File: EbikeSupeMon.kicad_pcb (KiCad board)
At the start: 2 copper layers, 47 parts, among them J1 USB_B_Micro, J2 Key switch, J3 Controller enable, J4 Bat IN, J5 Motor Out, Q1 DMP10H4D2S-7, SW1 IO_0, SW2 EN, SW3 USB-Reg_EN, U1 CP2102N-QFN28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

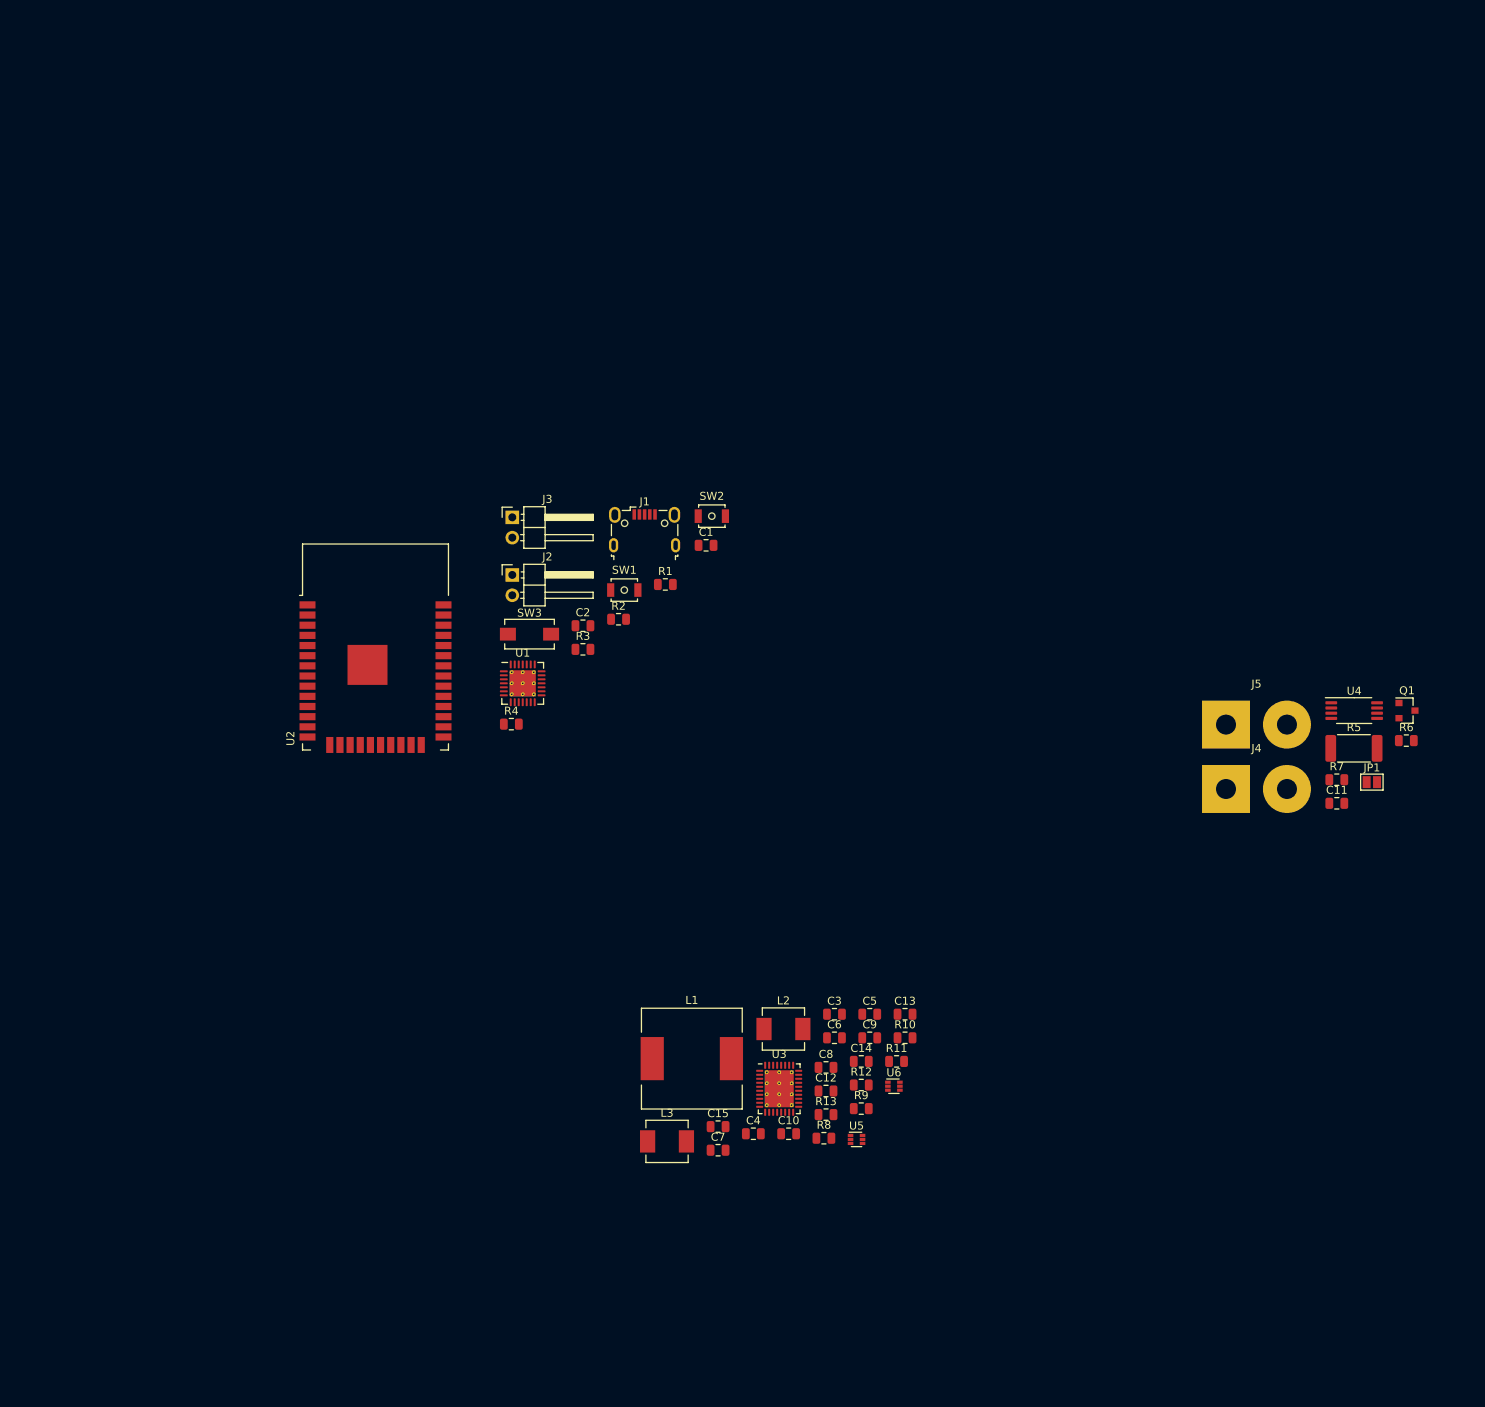
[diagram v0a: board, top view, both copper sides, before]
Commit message: 5v +3.3v reg layed out
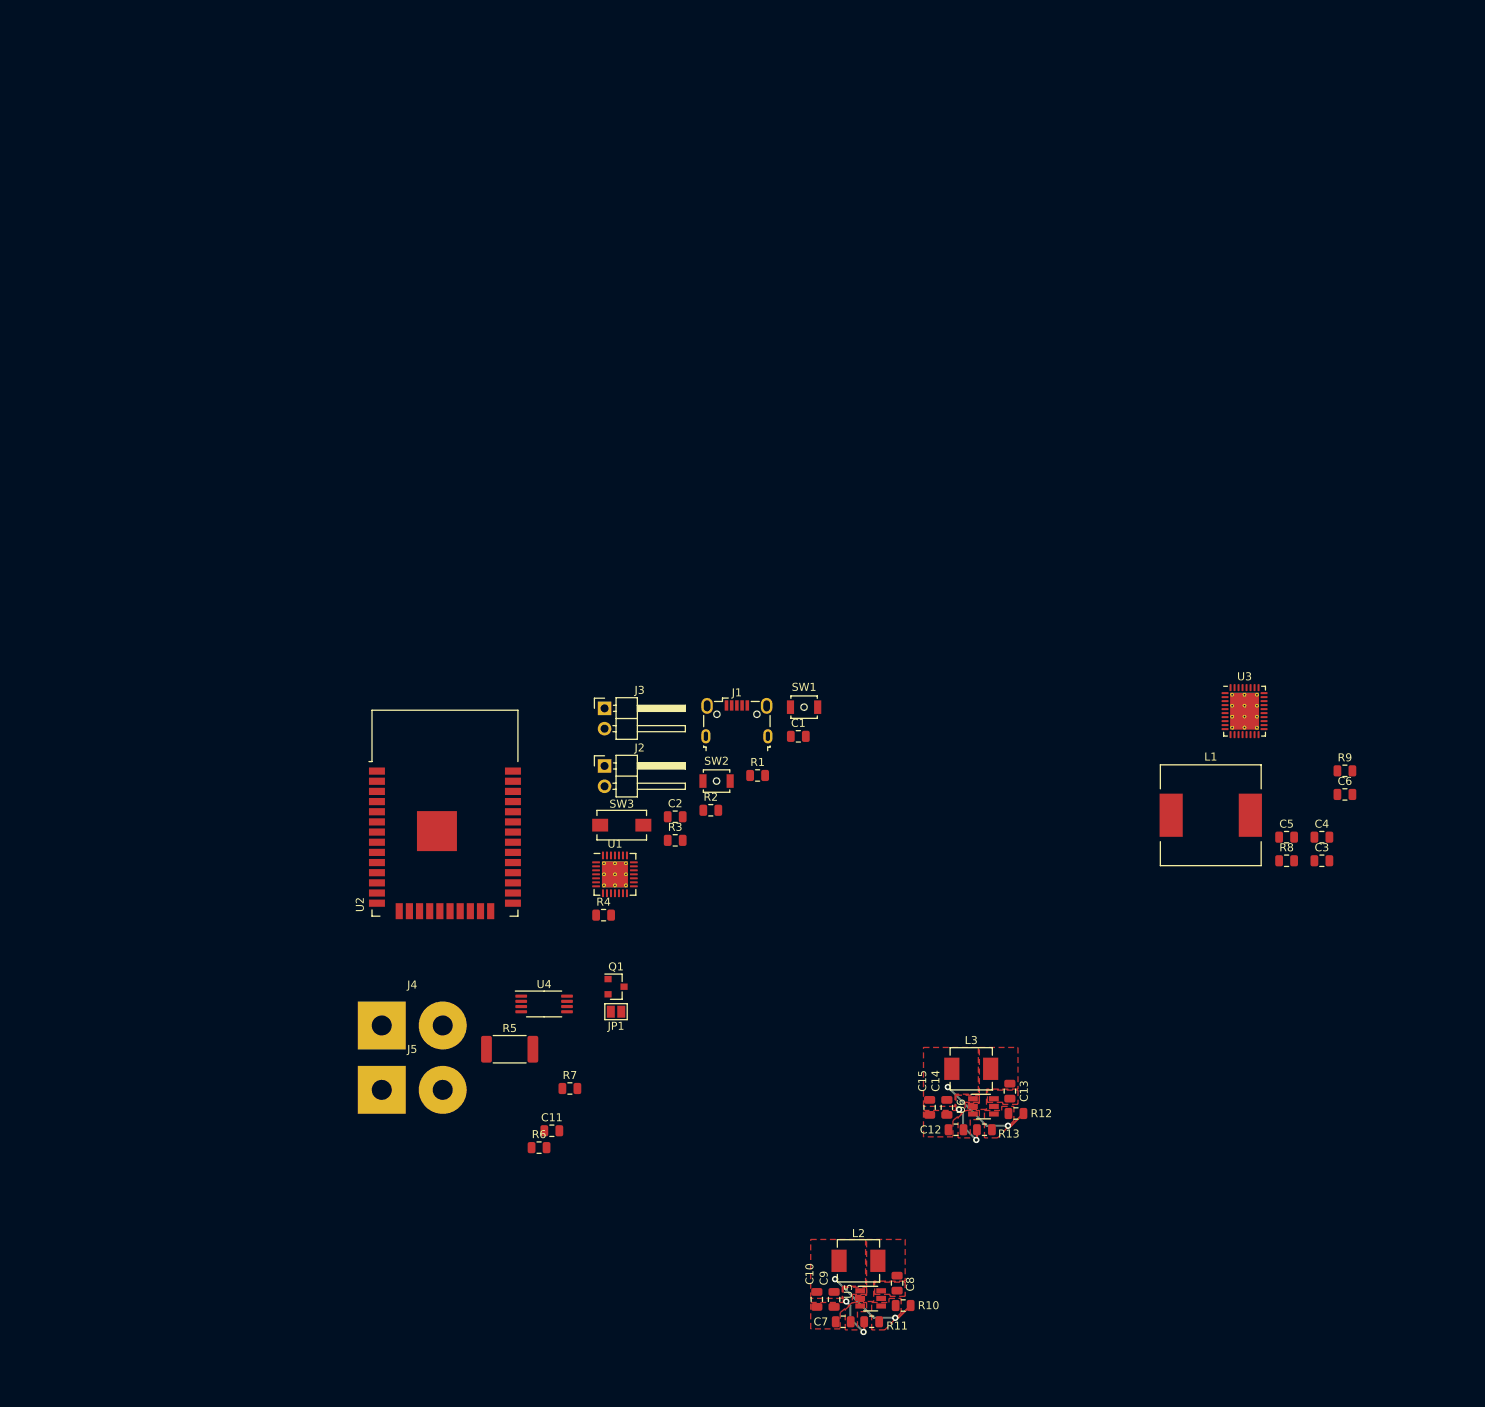
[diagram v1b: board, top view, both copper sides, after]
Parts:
- C10, C9: value 100nF X5R 6V -> 22uF X7R 10v
- C12: value 22uF X7R 10v -> 10uF 12V
- C13: value 22uF X7R 10v -> 100nF X5R 6V
- C8: value 10uF 12V -> 100nF X5R 6V
- R10: value 52.3k -> 31.6k
- R12: value 31.6k -> 52.3k
- U5, U6: footprint Package_TO_SOT_SMD:SOT-563 -> Package_TO_SOT_SMD:TSOT-23-6
- moved R6 119.8 mm to (112.3, 168.7)
- moved J5 115.0 mm to (92.7, 161.5)
- moved R5 112.0 mm to (108.7, 156.4)
- moved J4 109.6 mm to (92.7, 153.5)
- moved U4 107.7 mm to (113.0, 150.8)
- moved C11 106.3 mm to (113.9, 166.6)
- moved Q1 104.7 mm to (122.0, 148.6)
- moved R7 103.3 mm to (116.2, 161.3)
- moved JP1 98.7 mm to (122.0, 151.7), turned to 180 degrees
- moved C4 80.2 mm to (210.2, 129.9)
- moved U3 74.9 mm to (200.5, 114.2)
- moved R9 73.7 mm to (213.1, 121.6)
- moved L1 71.6 mm to (196.3, 127.2)
- moved C6 70.7 mm to (213.1, 124.6)
- moved R8 67.4 mm to (205.8, 132.9)
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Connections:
- C10 pad 1: Net-(C10-Pad1) -> +3V3
- C10 pad 2: Net-(C10-Pad2) -> GND
- C12 pad 1: +5V -> +12V
- C13 pad 1: +3V3 -> Net-(C13-Pad1)
- C13 pad 2: GND -> Net-(C13-Pad2)
- C15 pad 1: +3V3 -> +5V
- C8 pad 1: +12V -> Net-(C8-Pad1)
- C8 pad 2: GND -> Net-(C8-Pad2)
- C9 pad 1: Net-(C9-Pad1) -> +3V3
- C9 pad 2: Net-(C9-Pad2) -> GND
- J5 pad 2: (no net) -> Net-(J5-Pad2)
- L2 pad 1: Net-(C9-Pad2) -> Net-(C8-Pad2)
- L2 pad 2: +5V -> +3V3
- L3 pad 1: Net-(C10-Pad2) -> Net-(C13-Pad2)
- L3 pad 2: +3V3 -> +5V
- R10 pad 1: +5V -> +3V3
- R12 pad 1: +3V3 -> +5V
- U4 pad 3: (no net) -> Net-(R5-Pad3)
- U5 pad 1: +12V -> GND
- U5 pad 2: Net-(C9-Pad2) -> Net-(C8-Pad2)
- U5 pad 3: GND -> +12V
- U5 pad 4: Net-(C9-Pad1) -> Net-(R10-Pad2)
- U5 pad 6: Net-(R10-Pad2) -> Net-(C8-Pad1)
- U6 pad 1: +12V -> GND
- U6 pad 2: Net-(C10-Pad2) -> Net-(C13-Pad2)
- U6 pad 3: GND -> +12V
- U6 pad 4: Net-(C10-Pad1) -> Net-(R12-Pad2)
- U6 pad 6: Net-(R12-Pad2) -> Net-(C13-Pad1)
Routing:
- net +3V3: track 0.00 -> 12.1 mm, vias 0 -> 2
- net +5V: track 0.00 -> 12.1 mm, vias 0 -> 2
- net GND: track 0.00 -> 12.0 mm, vias 0 -> 4
- added copper zone on F.Cu, net +12V
- added copper zone on F.Cu, net +3V3
- added copper zone on F.Cu, net +5V
- added copper zone on F.Cu, net GND
- added copper zone on F.Cu, net Net-(C13-Pad1)
- added copper zone on F.Cu, net Net-(C13-Pad2)
- added copper zone on F.Cu, net Net-(C8-Pad1)
- added copper zone on F.Cu, net Net-(C8-Pad2)
- added copper zone on F.Cu, net Net-(R10-Pad2)
- added copper zone on F.Cu, net Net-(R12-Pad2)
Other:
- net class thin added: clearance 0.05, trace_width 0.2, via_dia 0.65, via_drill 0.3
- rule pad_to_mask_clearance: 0.05 -> 0.025
- rule trace_min: 0.2 -> 0.1

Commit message: 12vReg done
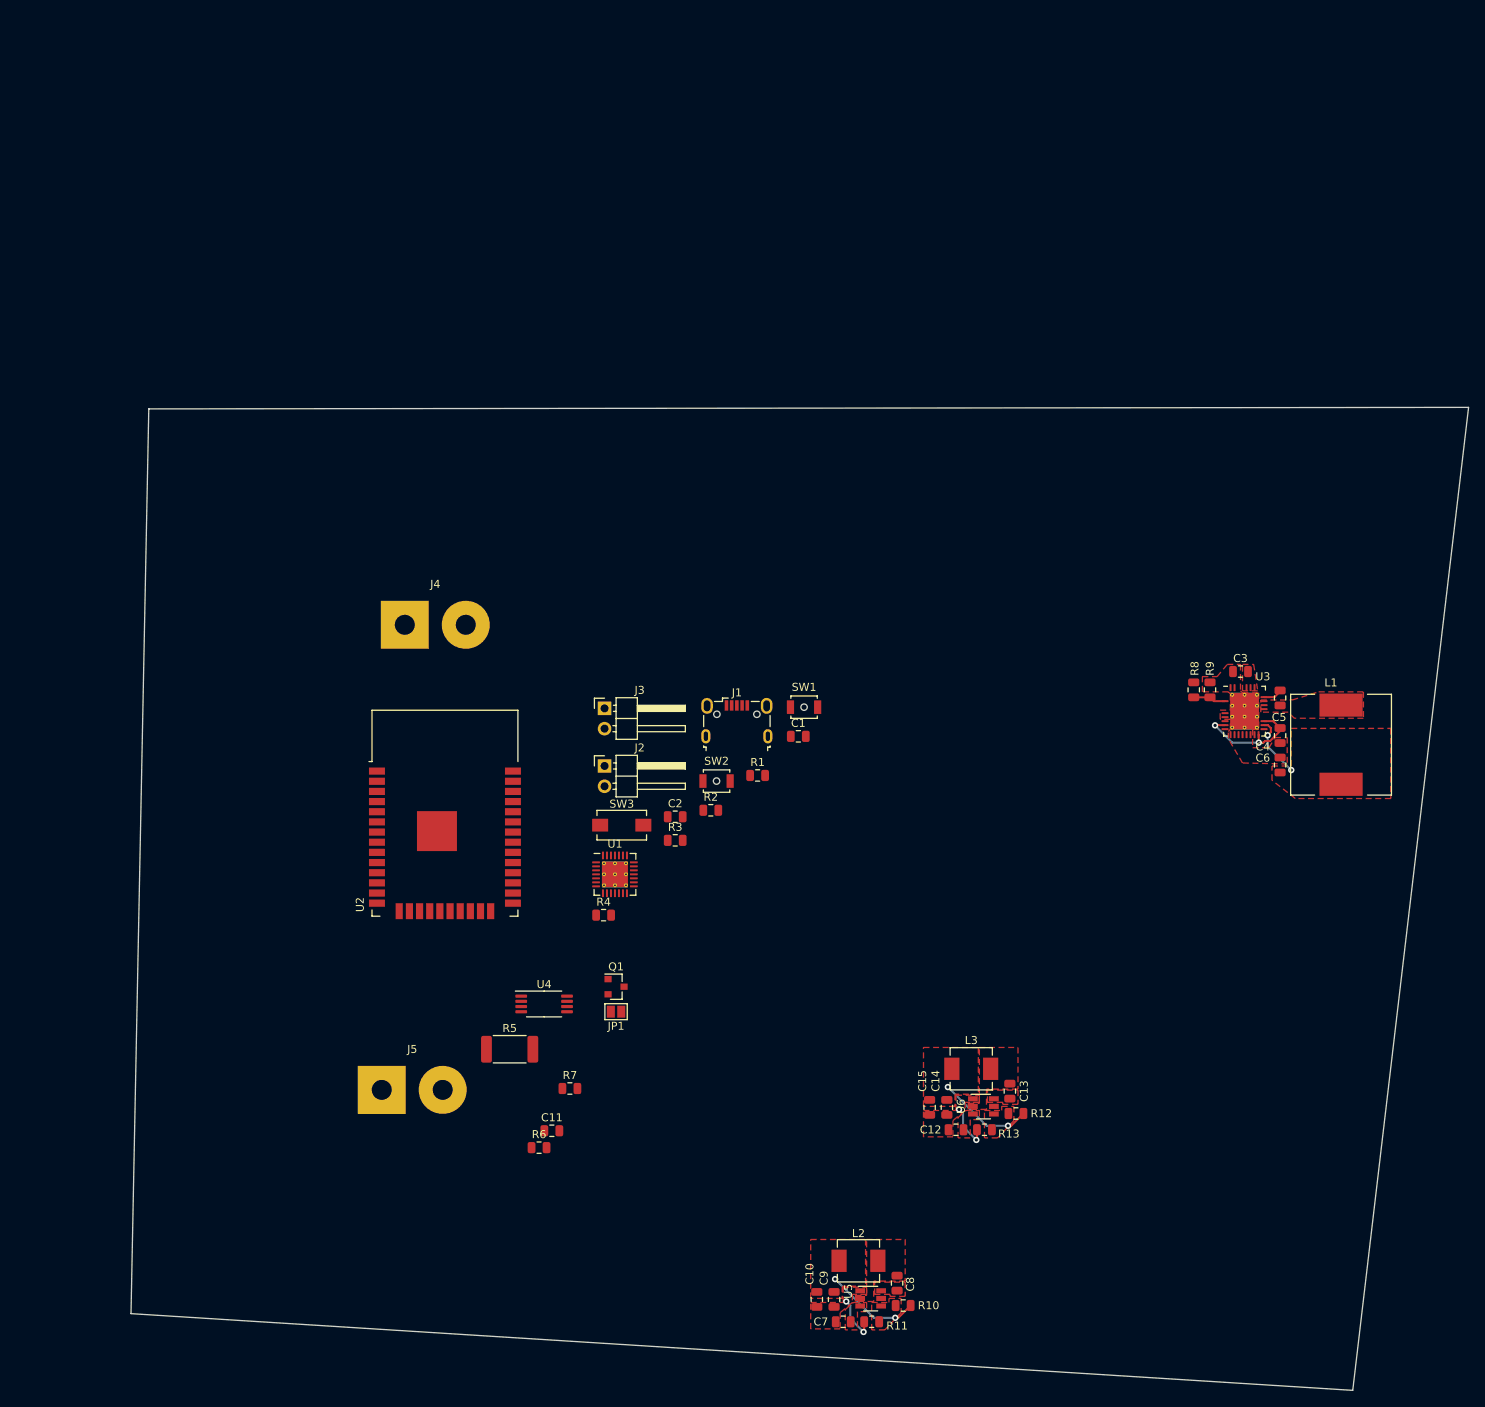
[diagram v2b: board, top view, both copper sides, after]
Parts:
- moved J4 50.2 mm to (95.6, 103.4)
- moved C3 25.7 mm to (200.0, 109.2), turned to 180 degrees
- moved R8 24.3 mm to (194.2, 111.5), turned to 90 degrees
- moved R9 19.7 mm to (196.2, 111.5), turned to 270 degrees
- moved L1 18.5 mm to (212.6, 118.4), turned to 270 degrees
- moved C5 17.4 mm to (205.0, 112.5), turned to 270 degrees
- moved C4 13.7 mm to (205.0, 117.2), turned to 270 degrees
- moved C6 8.90 mm to (205.0, 120.9), turned to 90 degrees
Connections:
- U3 pad 37: (no net) -> GND
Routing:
- net Net-(C4-Pad1): track 0.00 -> 14.6 mm, vias 0 -> 2
- net +12V: track 0.00 -> 7.64 mm, vias 0 -> 2
- net Net-(R8-Pad1): track 0.00 -> 4.11 mm
- net Net-(C5-Pad1): track 0.00 -> 2.48 mm
- added copper zone on F.Cu, net /Sheet5F3EA405/VBatt
- added copper zone on F.Cu, net Net-(C5-Pad2)
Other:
- board outline added: 167.2 x 122.9 mm

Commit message: layout proper started
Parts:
- moved L1 149.7 mm to (75.0, 59.3), turned to 0 degrees
- moved C5 143.2 mm to (69.2, 66.9), turned to 0 degrees
- moved C4 140.4 mm to (73.9, 66.9), turned to 0 degrees
- moved C3 139.2 mm to (65.9, 71.9), turned to 270 degrees
- moved C6 138.4 mm to (77.6, 66.9), turned to 180 degrees
- moved U3 136.6 mm to (70.8, 71.4), turned to 90 degrees
- moved R9 133.0 mm to (68.2, 75.7), turned to 0 degrees
- moved R8 130.5 mm to (68.2, 77.7), turned to 180 degrees
- moved U1 111.7 mm to (188.5, 44.9)
- moved C2 105.7 mm to (189.9, 40.7)
- moved R3 101.5 mm to (191.5, 50.0)
- moved JP1 98.9 mm to (187.9, 78.0)
- moved J1 98.1 mm to (188.4, 31.8)
- moved Q1 98.0 mm to (183.9, 72.7)
- moved R1 94.4 mm to (190.8, 42.9)
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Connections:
- R5 pad 2: Net-(R5-Pad2) -> /Sheet5F3EA405/VBatt
- R5 pad 3: Net-(R5-Pad3) -> Net-(J5-Pad2)
- U4 pad 2: Net-(R5-Pad2) -> /Sheet5F3EA405/VBatt
- U4 pad 3: Net-(R5-Pad3) -> Net-(J5-Pad2)
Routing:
- net /EN-5v: track 0.00 -> 14.4 mm
- net Net-(J2-Pad1): track 0.00 -> 10.1 mm
- net Net-(J5-Pad2): track 0.00 -> 5.07 mm
- net /Sheet5F3EA405/VBatt: track 0.00 -> 5.07 mm
- net GND: vias 4 -> 55
- added copper zone on B.Cu, net GND
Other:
- board outline removed

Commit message: rev 2 done
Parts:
- removed JP1: USB FET BYPASS, Jumper:SolderJumper-2_P1.3mm_Open_Pad1.0x1.5mm
- removed Q1: DMP10H4D2S-7, Package_TO_SOT_SMD:SOT-23
- added J6: USB_A, Connector_USB:USB_A_CONNFLY_DS1095-WNR0, F.Cu at (99.1, 54.5)
- moved C12 133.2 mm to (83.9, 60.4), turned to 90 degrees
- moved C7 132.7 mm to (83.9, 75.7), turned to 90 degrees
- moved R13 132.7 mm to (83.9, 63.9), turned to 90 degrees
- moved R11 131.5 mm to (83.9, 79.2), turned to 90 degrees
- moved C10 130.2 mm to (86.7, 72.4), turned to 180 degrees
- moved C15 130.1 mm to (86.7, 57.1), turned to 180 degrees
- moved C14 129.6 mm to (86.7, 59.2), turned to 180 degrees
- moved R12 129.4 mm to (85.9, 67.9), turned to 90 degrees
- moved C9 129.3 mm to (86.7, 74.5), turned to 180 degrees
- moved U6 128.6 mm to (86.8, 63.8), turned to 270 degrees
- moved R10 127.5 mm to (85.9, 83.2), turned to 90 degrees
- moved U5 127.5 mm to (86.8, 79.1), turned to 270 degrees
- moved C13 125.5 mm to (88.7, 67.1), turned to 0 degrees
- moved C8 123.9 mm to (88.7, 82.4), turned to 0 degrees
- moved L3 122.2 mm to (91.5, 62.3), turned to 90 degrees
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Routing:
- net +3V3: track 12.1 -> 83.3 mm, vias 2 -> 3
- net /DTR: track 0.00 -> 54.2 mm, vias 0 -> 2
- net /BattVRead: track 0.00 -> 47.7 mm
- net /12V_I_mon: track 0.00 -> 45.0 mm
- net /Isense: track 0.00 -> 43.8 mm
- net /RXD0: track 0.00 -> 43.7 mm, vias 0 -> 2
- net /TXD0: track 0.00 -> 41.7 mm, vias 0 -> 2
- net VBUS: track 0.00 -> 35.8 mm
- net /EN-5v: track 14.4 -> 49.7 mm, vias 0 -> 1
- net /EN: track 0.00 -> 30.9 mm, vias 0 -> 2
- net +5V: track 12.1 -> 21.9 mm
- net Net-(R1-Pad1): track 0.00 -> 9.24 mm, vias 0 -> 2
- net /D+: track 0.00 -> 9.19 mm, vias 0 -> 2
- net /D-: track 0.00 -> 9.07 mm
- net +12V: track 7.64 -> 16.5 mm, vias 2 -> 3
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- added copper zone on B.Cu, net /Sheet5F3EA405/VBatt
- added copper zone on B.Cu, net Net-(J5-Pad2)
- added copper zone on F.Cu, net Net-(J5-Pad2)
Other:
- board outline added: 69.8 x 58.4 mm
- board text added: "+"
- board text added: "- +"
- board text added: "5V^3A"
- board text added: "<3.3v"
- board text added: "<5v"
- board text added: "EN"
- board text added: "IO0"
- board text added: "POWER ME! +"
